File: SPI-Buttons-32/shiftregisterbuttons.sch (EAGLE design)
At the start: 44 parts, among them IC1 74AC165D, IC2 74AC165D, IC3 74AC165D, IC4 74AC165D

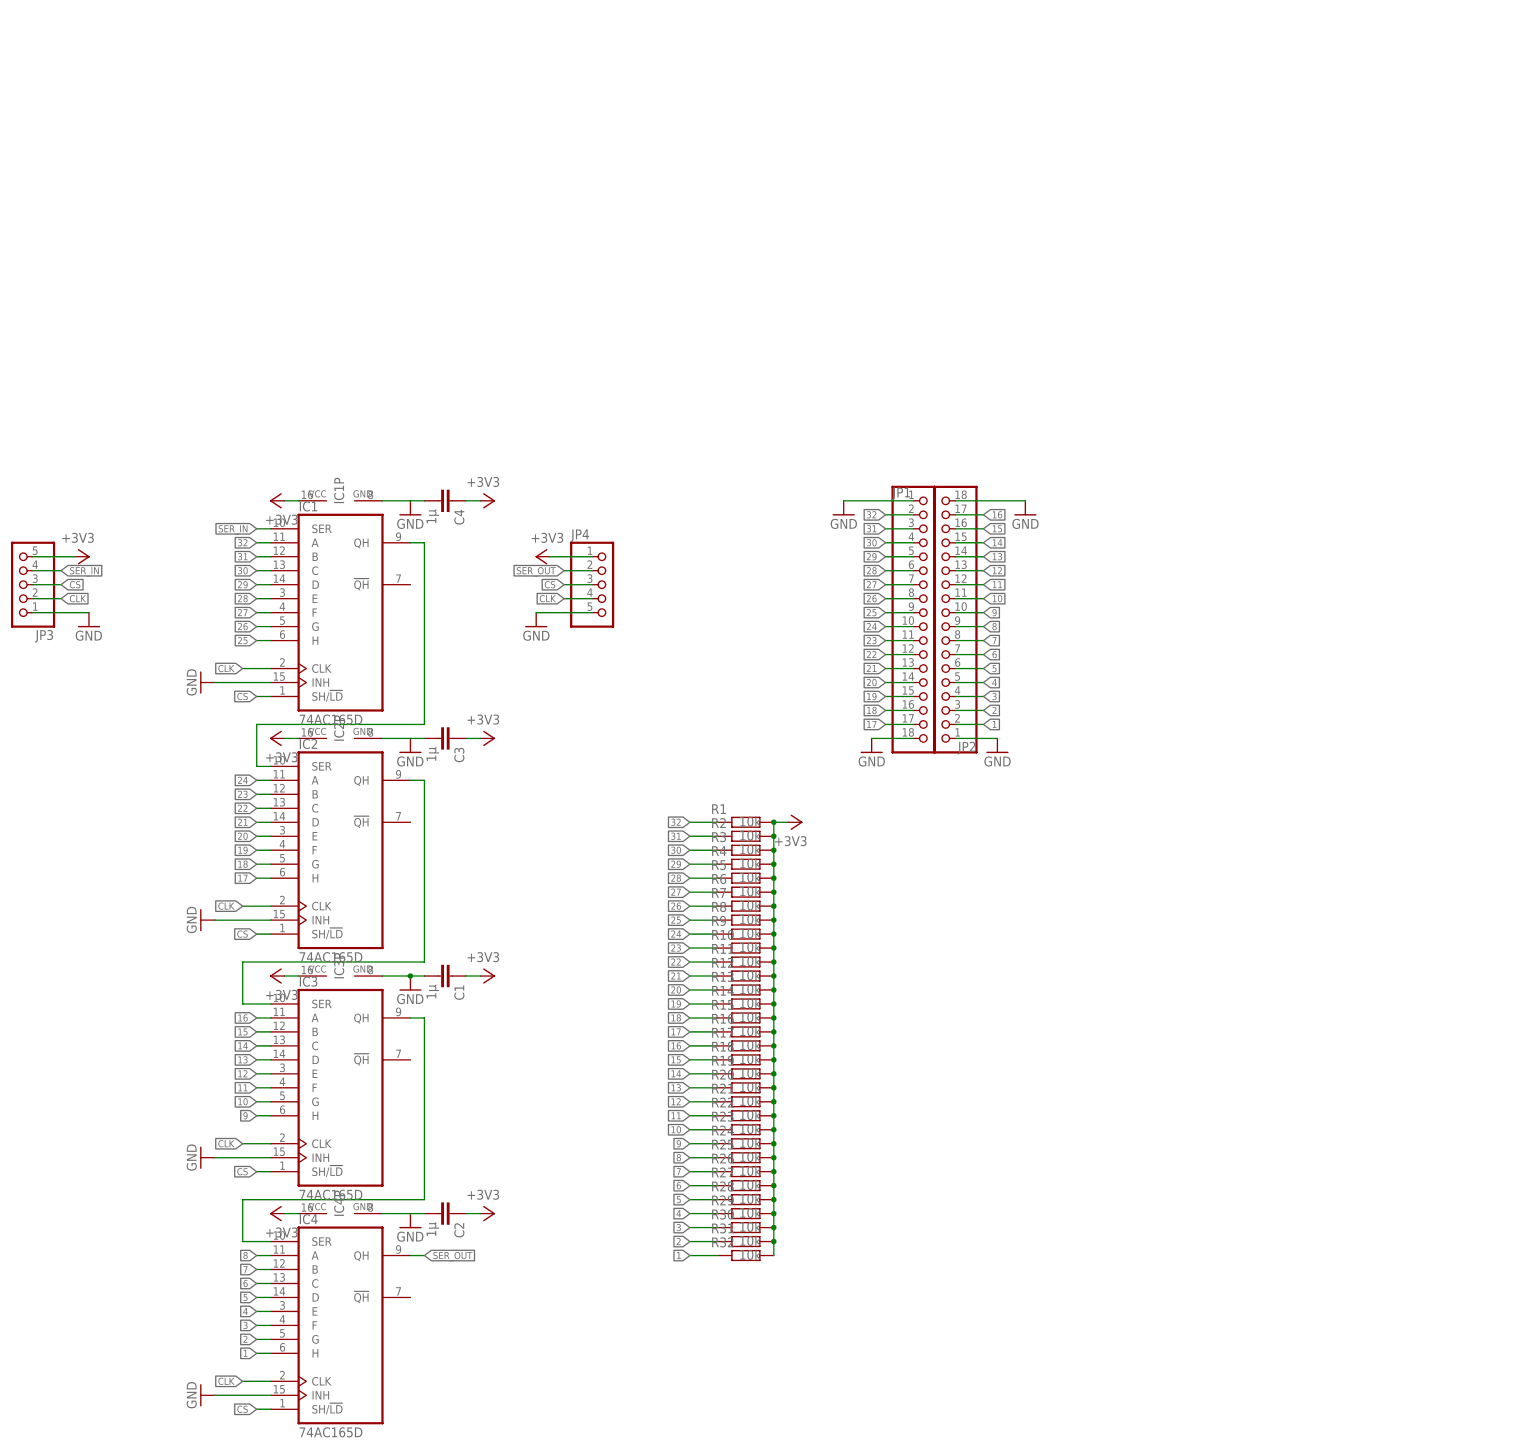
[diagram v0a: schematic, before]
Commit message: Updated SPI buttons to v1.2
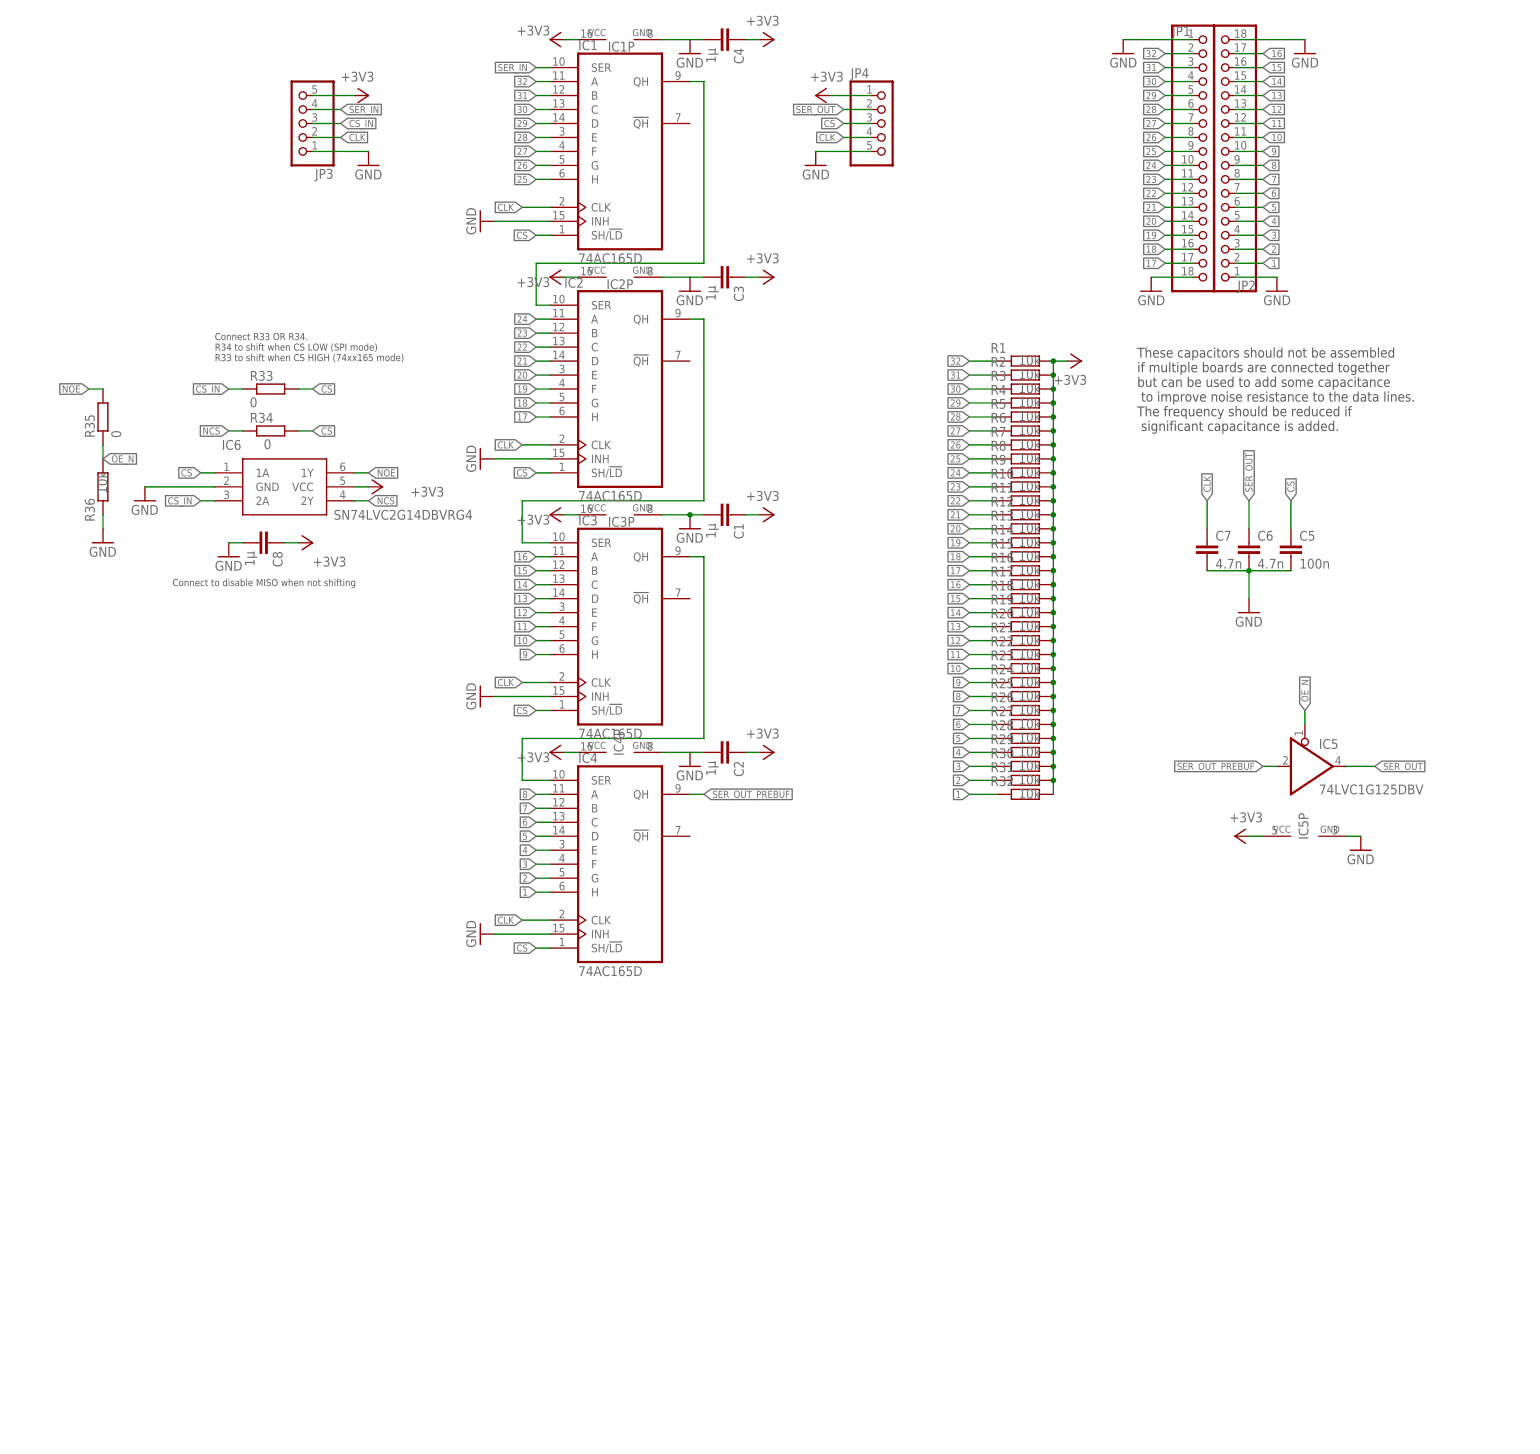
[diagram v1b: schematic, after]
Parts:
- added C5: 100n, resistor:C-EUC0603
- added C6, C7: 4.7n, resistor:C-EUC0603
- added C8: 1µ, resistor:C-EUC0603
- added IC5: 74LVC1G125DBV, 74xx-little-de:74LVC1G125DBV
- added IC6: SN74LVC2G14DBVRG4, SamacSys_Parts:SN74LVC2G14DBVRG4
- added R33, R34, R35: 0, resistor:R-EU_R0603
- added R36: 10k, resistor:R-EU_R0603
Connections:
- new net CS_IN: IC6.2A, JP3.3, R33.1
- new net NCS: IC6.2Y, R34.1
- new net NOE: IC6.1Y, R35.2
- new net OE_N: IC5A.OE, R35.1, R36.2
- new net SER_OUT_PREBUF: IC4A.QH, IC5A.I
- net +3V3: now also C8.1, IC5P.VCC, IC6.VCC
- net CLK: now also C7.1
- net CS: now also C5.1, IC6.1A, R33.2, R34.2; no longer JP3.3
- net GND: now also C5.2, C6.2, C7.2, C8.2, IC5P.GND, IC6.GND, R36.1
- net SER_OUT: now also C6.1, IC5A.O; no longer IC4A.QH
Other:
- note added: "Connect R33 OR R34. R34 to shift when CS LOW (SPI mode) R33 to shift when CS HIGH (74xx165 mode)"
- note added: "Connect to disable MISO when not shifting"
- note added: "These capacitors should not be assembled if multiple boards are connected together but can be used to add some capacitance to improve noise resistance to the data lines. The frequency should be reduced if significant capacitance is added."
- moved on the sheet: C1, C2, C3, C4, IC1, IC1P, IC2, IC2P, IC3, IC3P, IC4, IC4P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
